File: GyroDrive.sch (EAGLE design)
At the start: 41 parts, among them IC1 AD8235, IC2 AD8235, IC3 AD8235, IC4 AD8235

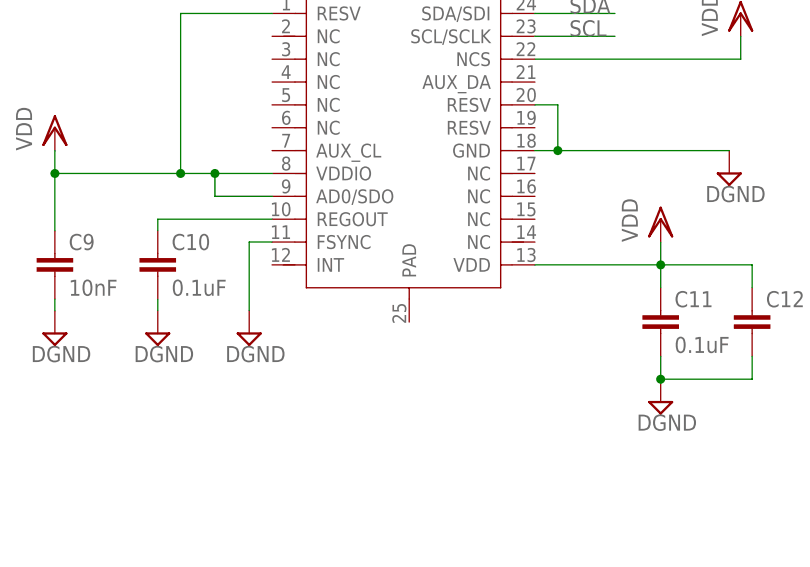
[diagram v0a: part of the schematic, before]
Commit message: Removed copper from underneath MPU-9250
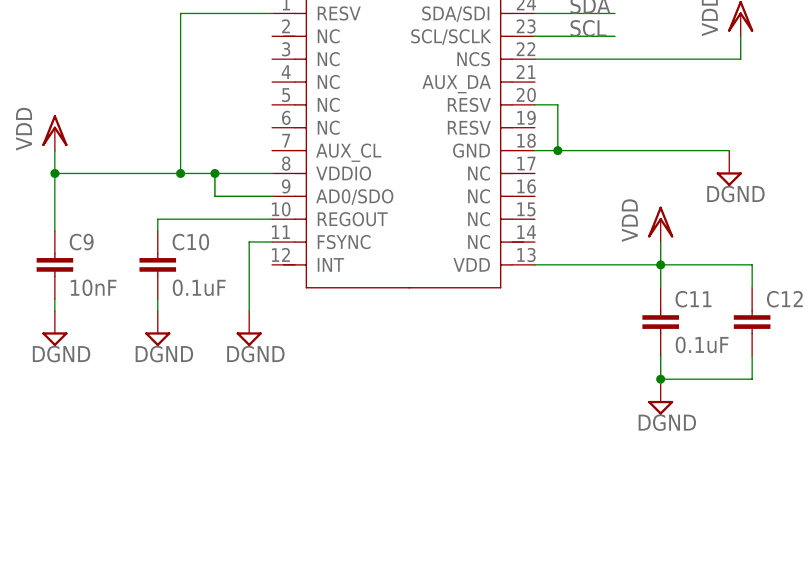
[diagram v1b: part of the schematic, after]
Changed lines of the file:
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@@
 <?xml version="1.0" encoding="utf-8"?>
 <!DOCTYPE eagle SYSTEM "eagle.dtd">
-<eagle version="7.5.0">
+<eagle version="7.4.0">
 <drawing>
 <settings>

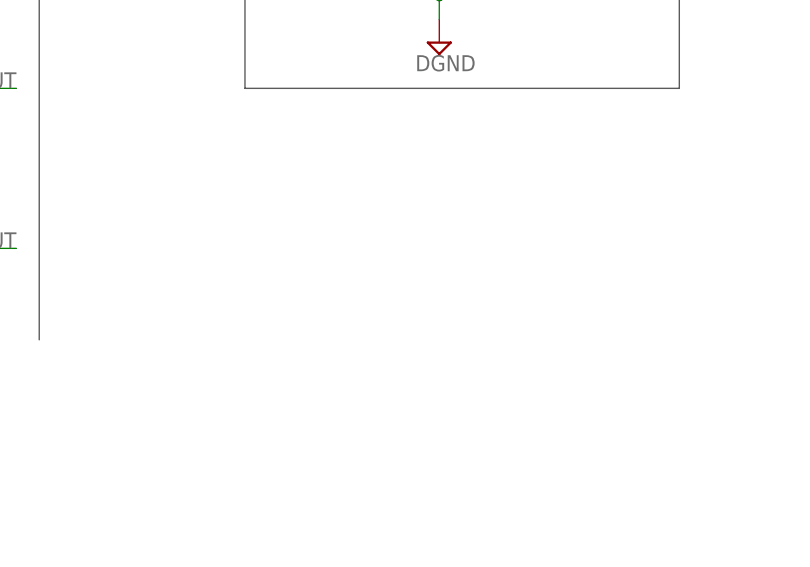
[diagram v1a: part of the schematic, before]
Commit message: Added jumper between VGND and AGND
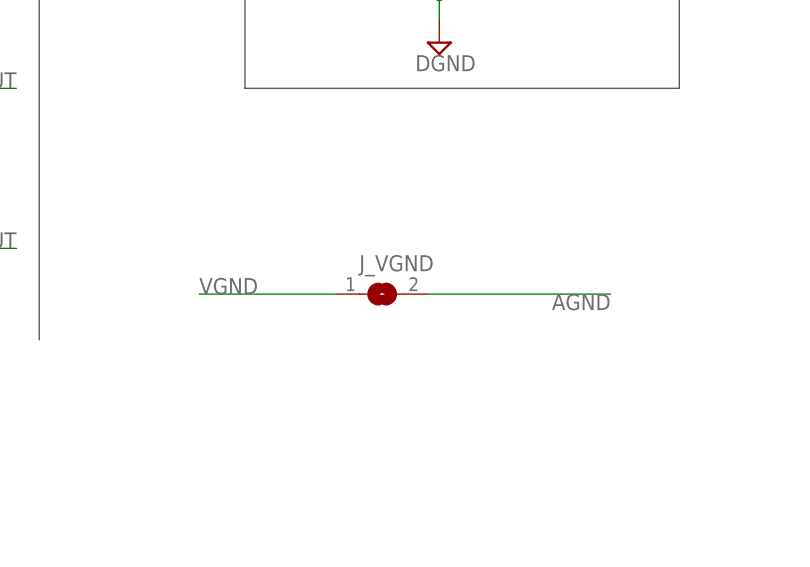
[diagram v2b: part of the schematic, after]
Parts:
- added J_VGND: (no value), michael-stetner:SJ
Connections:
- net AGND: now also J_VGND.2
- net VGND: now also J_VGND.1
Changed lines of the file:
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@@
 <part name="E4" library="michael-stetner" deviceset="THROUGH-HOLE-30MIL/15MIL" device=""/>
 <part name="VGND" library="michael-stetner" deviceset="THROUGH-HOLE-30MIL/15MIL" device=""/>
+<part name="J_VGND" library="michael-stetner" deviceset="SJ" device=""/>
 </parts>
 <sheets>
@@
 <attribute name="VALUE" x="161.417" y="-76.962" size="1.778" layer="96"/>
 </instance>
+<instance part="J_VGND" gate="1" x="106.68" y="-53.34"/>
 </instances>
 <busses>
@@
 <wire x1="332.74" y1="-71.12" x2="332.74" y2="-73.66" width="0.1524" layer="91"/>
 </segment>
+<segment>
+<pinref part="J_VGND" gate="1" pin="2"/>
+<wire x1="111.76" y1="-53.34" x2="132.08" y2="-53.34" width="0.1524" layer="91"/>
+<label x="132.08" y="-53.34" size="1.778" layer="95" rot="R180"/>
+</segment>
 </net>
 <net name="S1" class="0">
@@
 <wire x1="165.1" y1="-73.66" x2="180.34" y2="-73.66" width="0.1524" layer="91"/>
 </segment>
-</net>
+<segment>
+<pinref part="J_VGND" gate="1" pin="1"/>
+<wire x1="101.6" y1="-53.34" x2="86.36" y2="-53.34" width="0.1524" layer="91"/>
+<label x="86.36" y="-53.34" size="1.778" layer="95"/>
+</segment>
+</net>

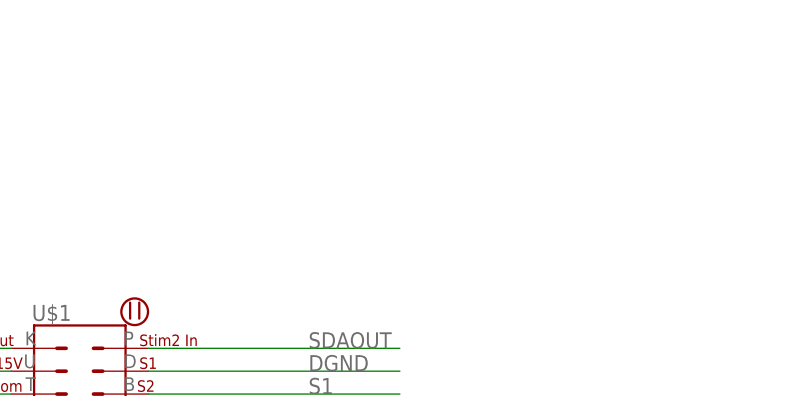
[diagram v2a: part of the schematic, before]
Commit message: Added attachment points for a grounding shield
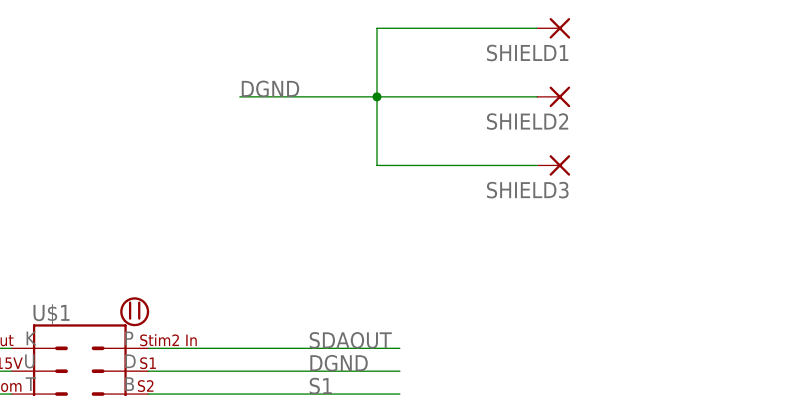
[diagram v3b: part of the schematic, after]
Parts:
- added SHIELD1, SHIELD2, SHIELD3: (no value), michael-stetner:SMD2
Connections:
- net DGND: now also SHIELD1.P, SHIELD2.P, SHIELD3.P
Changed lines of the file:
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@@
 <part name="VGND" library="michael-stetner" deviceset="THROUGH-HOLE-30MIL/15MIL" device=""/>
 <part name="J_VGND" library="michael-stetner" deviceset="SJ" device=""/>
+<part name="SHIELD1" library="michael-stetner" deviceset="SMD2" device=""/>
+<part name="SHIELD2" library="michael-stetner" deviceset="SMD2" device=""/>
+<part name="SHIELD3" library="michael-stetner" deviceset="SMD2" device=""/>
 </parts>
 <sheets>
@@
 </instance>
 <instance part="J_VGND" gate="1" x="106.68" y="-53.34"/>
+<instance part="SHIELD1" gate="1" x="81.28" y="68.58" rot="R180"/>
+<instance part="SHIELD2" gate="1" x="81.28" y="60.96" rot="R180"/>
+<instance part="SHIELD3" gate="1" x="81.28" y="53.34" rot="R180"/>
 </instances>
 <busses>
@@
 <label x="53.34" y="30.48" size="1.778" layer="95"/>
 </segment>
-</net>
+<segment>
+<pinref part="SHIELD1" gate="1" pin="P"/>
+<wire x1="78.74" y1="68.58" x2="60.96" y2="68.58" width="0.1524" layer="91"/>
+<wire x1="60.96" y1="68.58" x2="60.96" y2="60.96" width="0.1524" layer="91"/>
+<pinref part="SHIELD2" gate="1" pin="P"/>
+<wire x1="60.96" y1="60.96" x2="78.74" y2="60.96" width="0.1524" layer="91"/>
+<junction x="60.96" y="60.96"/>
+<pinref part="SHIELD3" gate="1" pin="P"/>
+<wire x1="60.96" y1="53.34" x2="78.74" y2="53.34" width="0.1524" layer="91"/>
+<wire x1="60.96" y1="53.34" x2="60.96" y2="60.96" width="0.1524" layer="91"/>
+<wire x1="60.96" y1="60.96" x2="45.72" y2="60.96" width="0.1524" layer="91"/>
+<label x="45.72" y="60.96" size="1.778" layer="95"/>
+</segment>
+</net>

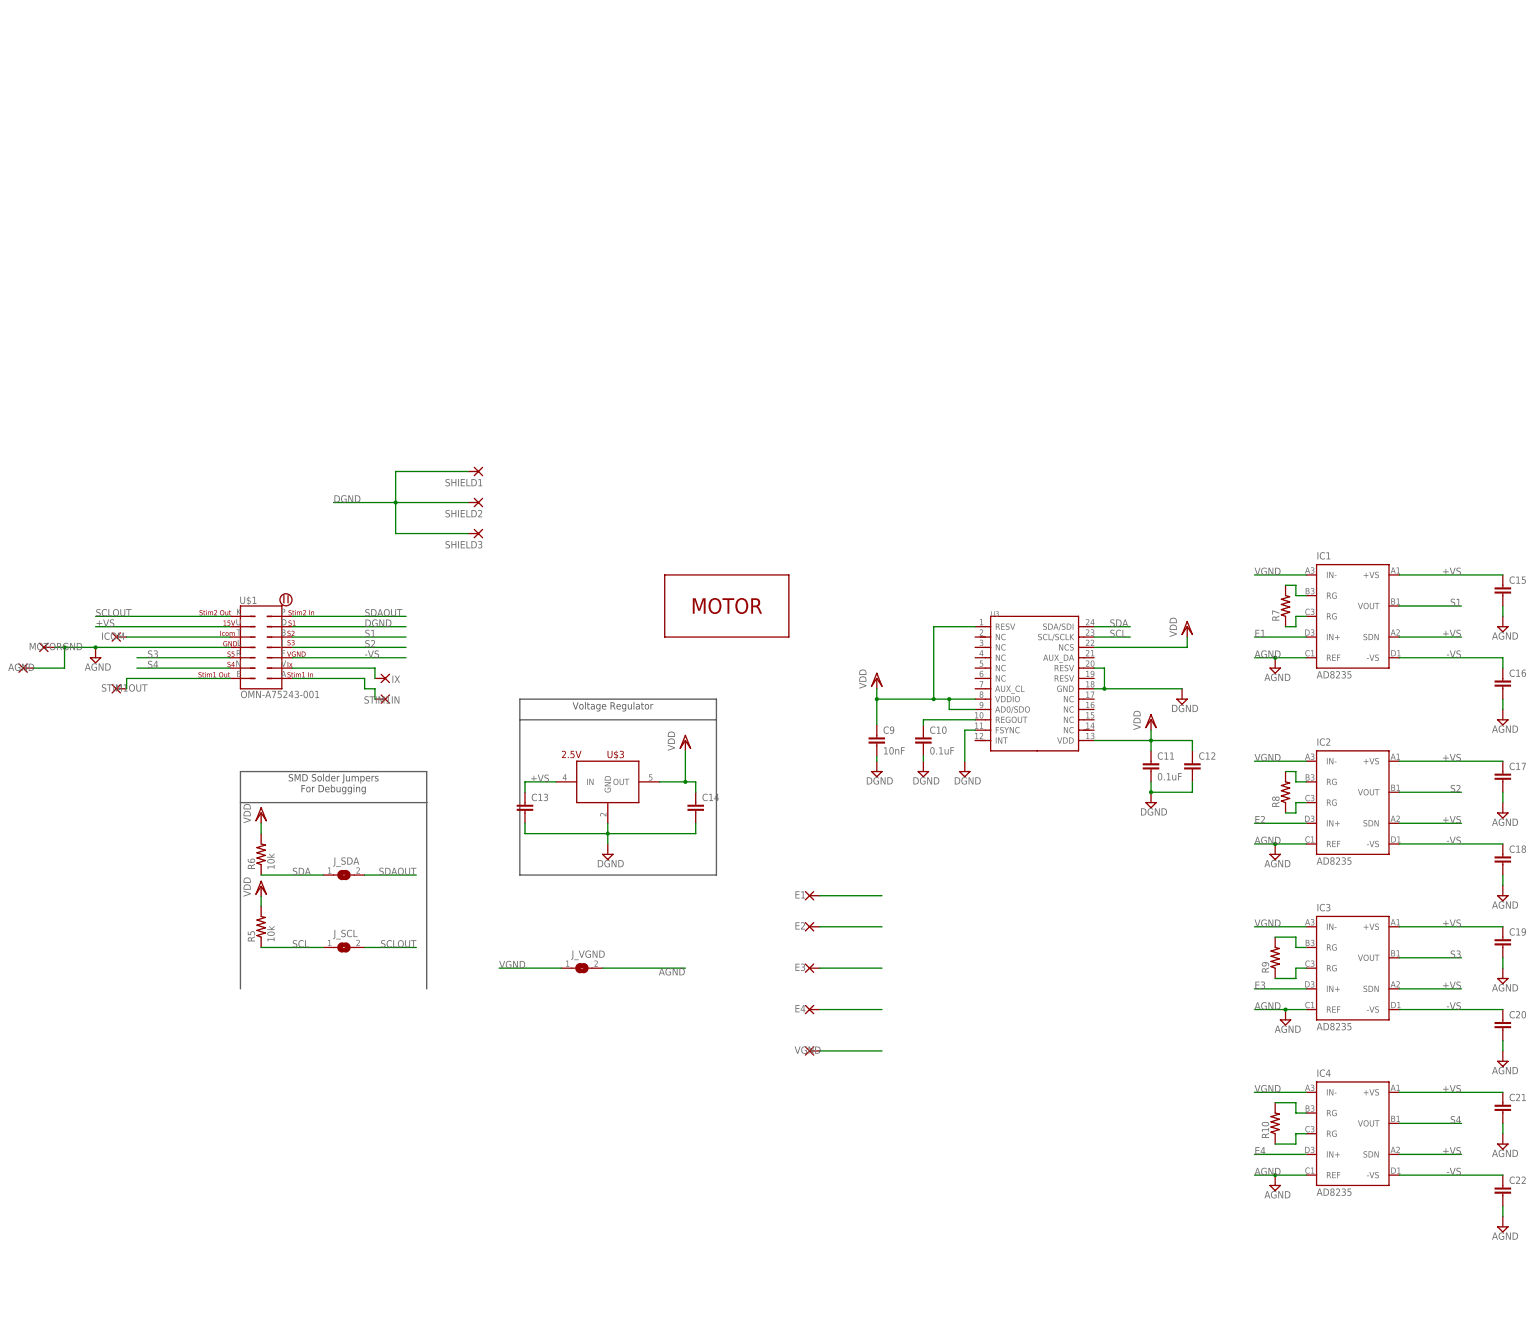
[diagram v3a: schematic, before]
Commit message: Made board more vertical - moved IMU up, and rotated instrumentation amplifier block by 90 degrees
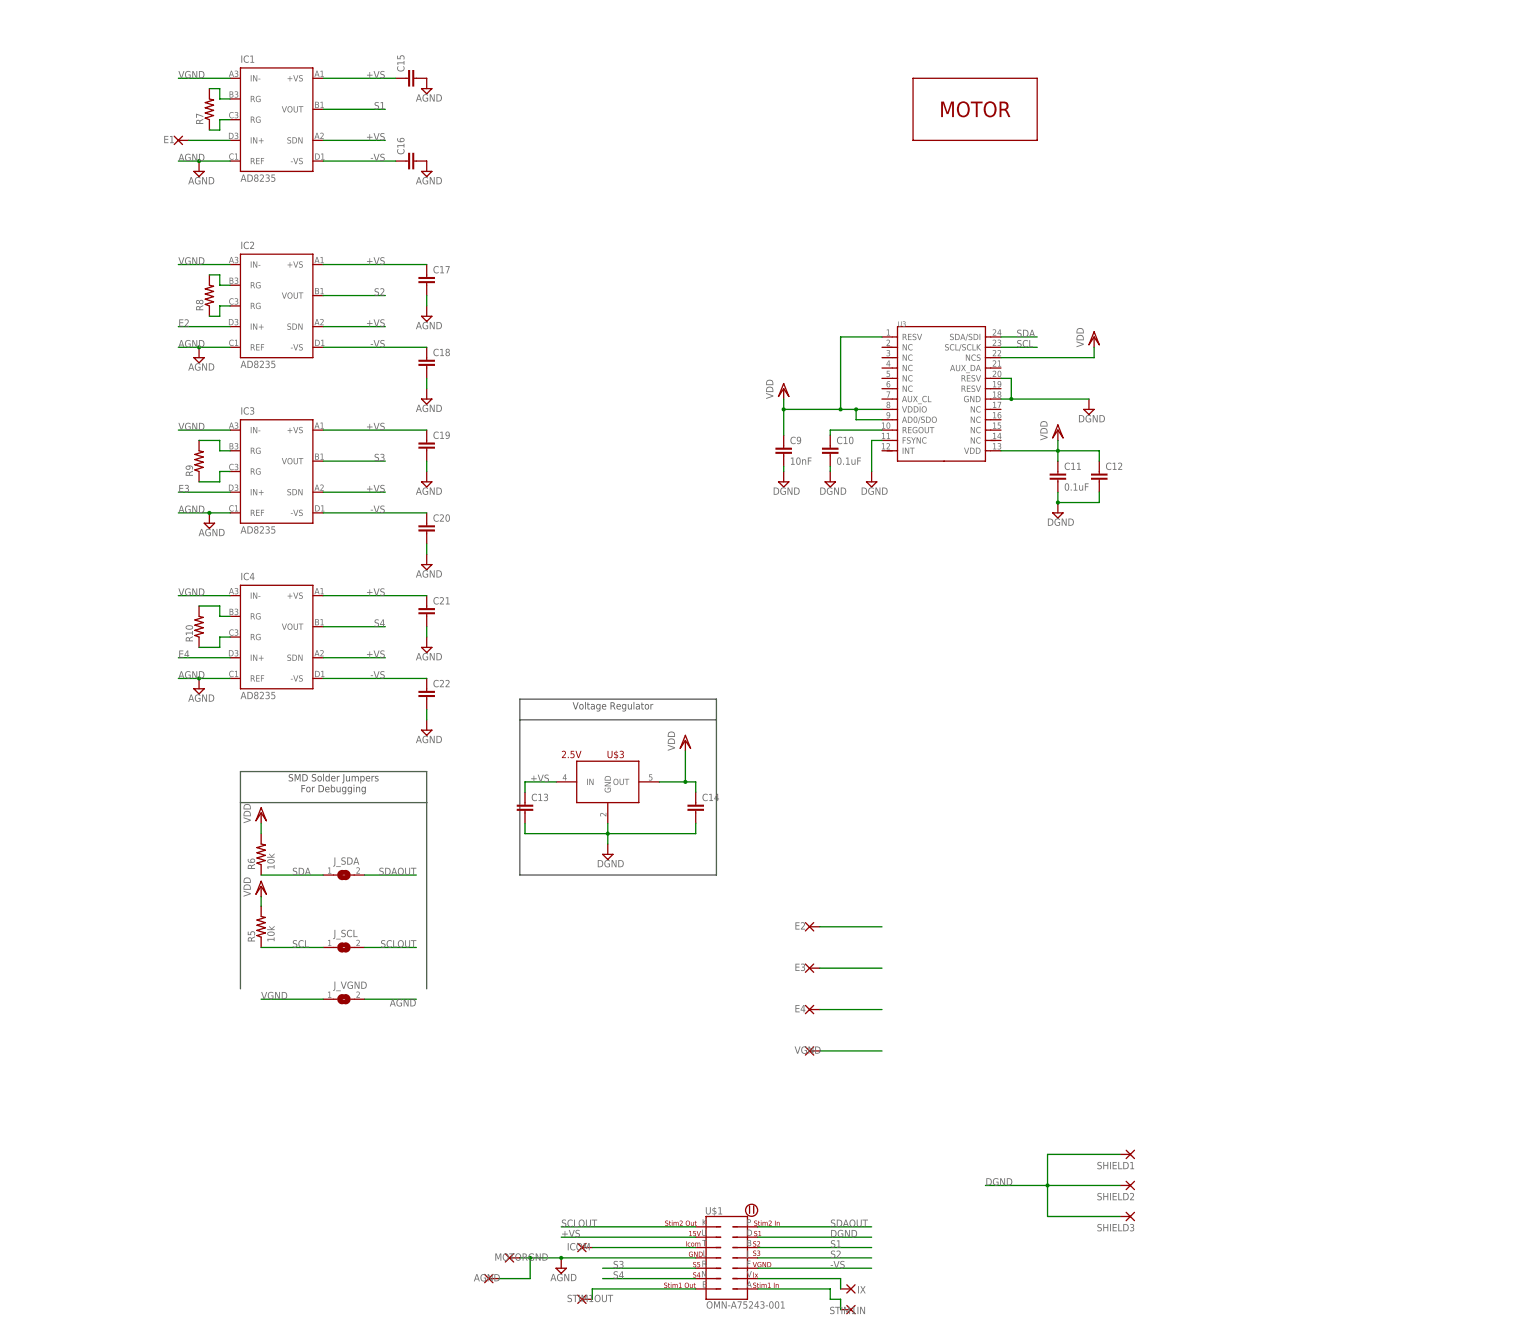
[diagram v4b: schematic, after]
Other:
- moved on the sheet: AGND, C10, C11, C12, C15, C16, C17, C18, C19, C20, C21, C22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

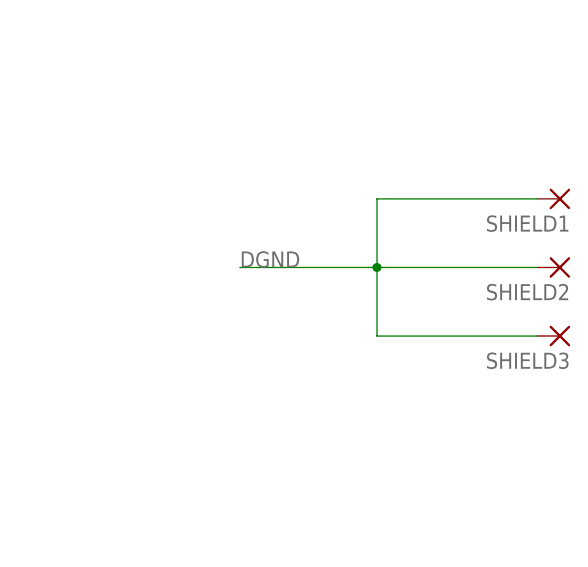
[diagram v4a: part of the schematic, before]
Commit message: Finished routing digital components
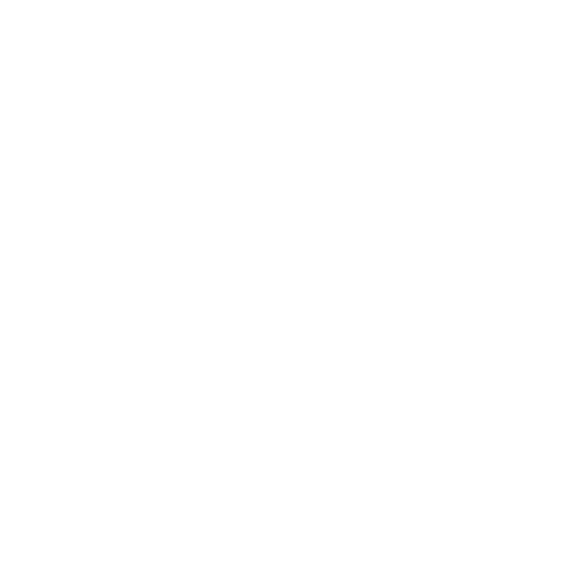
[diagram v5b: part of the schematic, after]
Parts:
- removed SHIELD1, SHIELD2, SHIELD3: (no value), michael-stetner:SMD2
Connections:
- net DGND: no longer SHIELD1.P, SHIELD2.P, SHIELD3.P
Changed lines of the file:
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@@
 <?xml version="1.0" encoding="utf-8"?>
 <!DOCTYPE eagle SYSTEM "eagle.dtd">
-<eagle version="7.4.0">
+<eagle version="7.5.0">
 <drawing>
 <settings>
@@
 <part name="VGND" library="michael-stetner" deviceset="THROUGH-HOLE-30MIL/15MIL" device=""/>
 <part name="J_VGND" library="michael-stetner" deviceset="SJ" device=""/>
-<part name="SHIELD1" library="michael-stetner" deviceset="SMD2" device=""/>
-<part name="SHIELD2" library="michael-stetner" deviceset="SMD2" device=""/>
-<part name="SHIELD3" library="michael-stetner" deviceset="SMD2" device=""/>
 <part name="FRAME1" library="frames" deviceset="LETTER_L" device=""/>
 </parts>
@@
 </instance>
 <instance part="J_VGND" gate="1" x="48.26" y="-60.96"/>
-<instance part="SHIELD1" gate="1" x="241.3" y="-99.06" rot="R180"/>
-<instance part="SHIELD2" gate="1" x="241.3" y="-106.68" rot="R180"/>
-<instance part="SHIELD3" gate="1" x="241.3" y="-114.3" rot="R180"/>
 <instance part="FRAME1" gate="G$1" x="0" y="0"/>
 <instance part="FRAME1" gate="G$2" x="147.32" y="0"/>
@@
 <label x="167.64" y="-119.38" size="1.778" layer="95"/>
 </segment>
-<segment>
-<pinref part="SHIELD1" gate="1" pin="P"/>
-<wire x1="238.76" y1="-99.06" x2="220.98" y2="-99.06" width="0.1524" layer="91"/>
-<wire x1="220.98" y1="-99.06" x2="220.98" y2="-106.68" width="0.1524" layer="91"/>
-<pinref part="SHIELD2" gate="1" pin="P"/>
-<wire x1="220.98" y1="-106.68" x2="238.76" y2="-106.68" width="0.1524" layer="91"/>
-<junction x="220.98" y="-106.68"/>
-<pinref part="SHIELD3" gate="1" pin="P"/>
-<wire x1="220.98" y1="-114.3" x2="238.76" y2="-114.3" width="0.1524" layer="91"/>
-<wire x1="220.98" y1="-114.3" x2="220.98" y2="-106.68" width="0.1524" layer="91"/>
-<wire x1="220.98" y1="-106.68" x2="205.74" y2="-106.68" width="0.1524" layer="91"/>
-<label x="205.74" y="-106.68" size="1.778" layer="95"/>
-</segment>
-</net>
+</net>
